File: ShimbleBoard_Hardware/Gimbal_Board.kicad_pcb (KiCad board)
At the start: 2 copper layers, 124.5 x 81.3 mm, 85 parts, among them Q1 Q_NMOS_GDS, Q2 Q_NMOS_GDS, Q3 Q_NMOS_GDS, Q4 Q_NMOS_GDS, Q5 Q_NMOS_GDS, Q6 Q_NMOS_GDS, Q7 Q_NMOS_GDS, Q8 Q_NMOS_GDS, SW1 SW_Push, SW10 SW_SPDT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

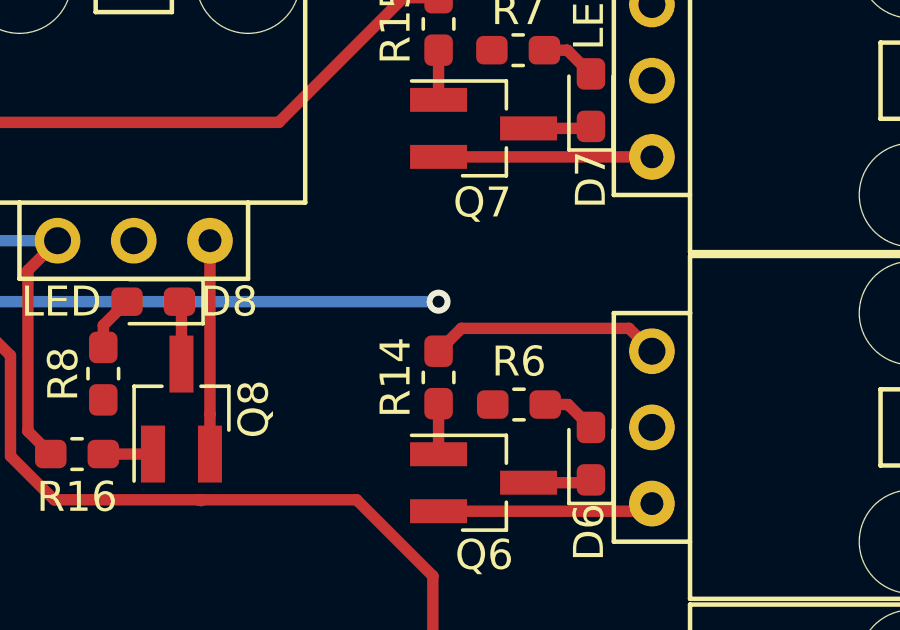
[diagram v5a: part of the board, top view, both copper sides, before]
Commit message: Added border that needs fixing
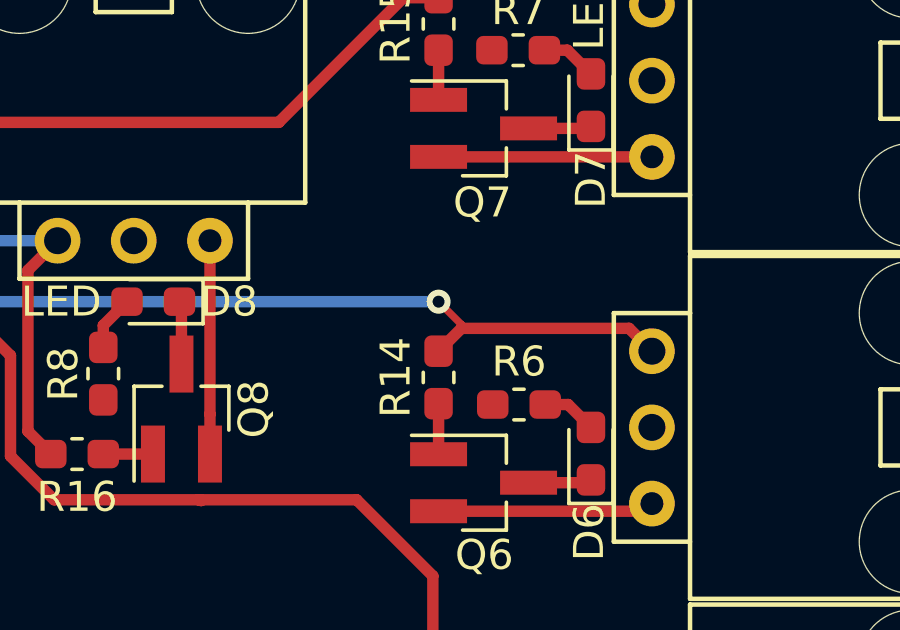
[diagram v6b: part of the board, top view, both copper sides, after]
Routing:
- net Servo_Ctrl_6: track 47.3 -> 48.5 mm
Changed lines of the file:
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@@
     (thickness 1.6)
     (drawings 18)
-    (tracks 408)
+    (tracks 410)
     (zones 0)
     (modules 85)
@@
   )
   (setup
-    (last_trace_width 0.381)
+    (last_trace_width 0.25)
     (user_trace_width 0.381)
     (user_trace_width 0.762)
@@
   (segment (start 157.734 65.786) (end 173.228 65.786) (width 0.381) (layer B.Cu) (net 11))
   (via (at 173.228 65.786) (size 0.8) (drill 0.4) (layers F.Cu B.Cu) (net 11))
+  (segment (start 173.99 66.548) (end 173.228 65.786) (width 0.25) (layer F.Cu) (net 11))
+  (segment (start 173.99 66.675) (end 173.99 66.548) (width 0.25) (layer F.Cu) (net 11))
   (segment (start 173.228 55.654) (end 173.99 54.892) (width 0.381) (layer F.Cu) (net 12))
   (segment (start 179.352 54.892) (end 180.34 55.88) (width 0.381) (layer F.Cu) (net 12))

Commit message: Fixed stuff
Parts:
- moved D16 0.06 mm to (159.5, 90.5)
- moved R22 0.06 mm to (149.3, 90.5)
- moved R23 0.06 mm to (156.1, 90.5)
- moved D10 0.06 mm to (119.1, 90.5)
- moved R17 0.06 mm to (115.7, 90.5)
- moved D11 0.06 mm to (125.8, 90.5)
- moved D12 0.06 mm to (132.6, 90.5)
- moved D13 0.06 mm to (139.3, 90.5)
- moved D14 0.06 mm to (146.0, 90.5)
- moved D15 0.06 mm to (152.8, 90.5)
- moved D9 0.06 mm to (112.4, 90.5)
- moved R18 0.06 mm to (122.4, 90.5)
- moved R19 0.06 mm to (129.1, 90.5)
- moved R20 0.06 mm to (135.9, 90.5)
- moved R21 0.06 mm to (142.6, 90.5)
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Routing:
- net GND: track 169.3 -> 175.0 mm
- net Servo_SW_1: track 36.1 -> 36.9 mm
